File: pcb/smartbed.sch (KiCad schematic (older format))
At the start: 1 part

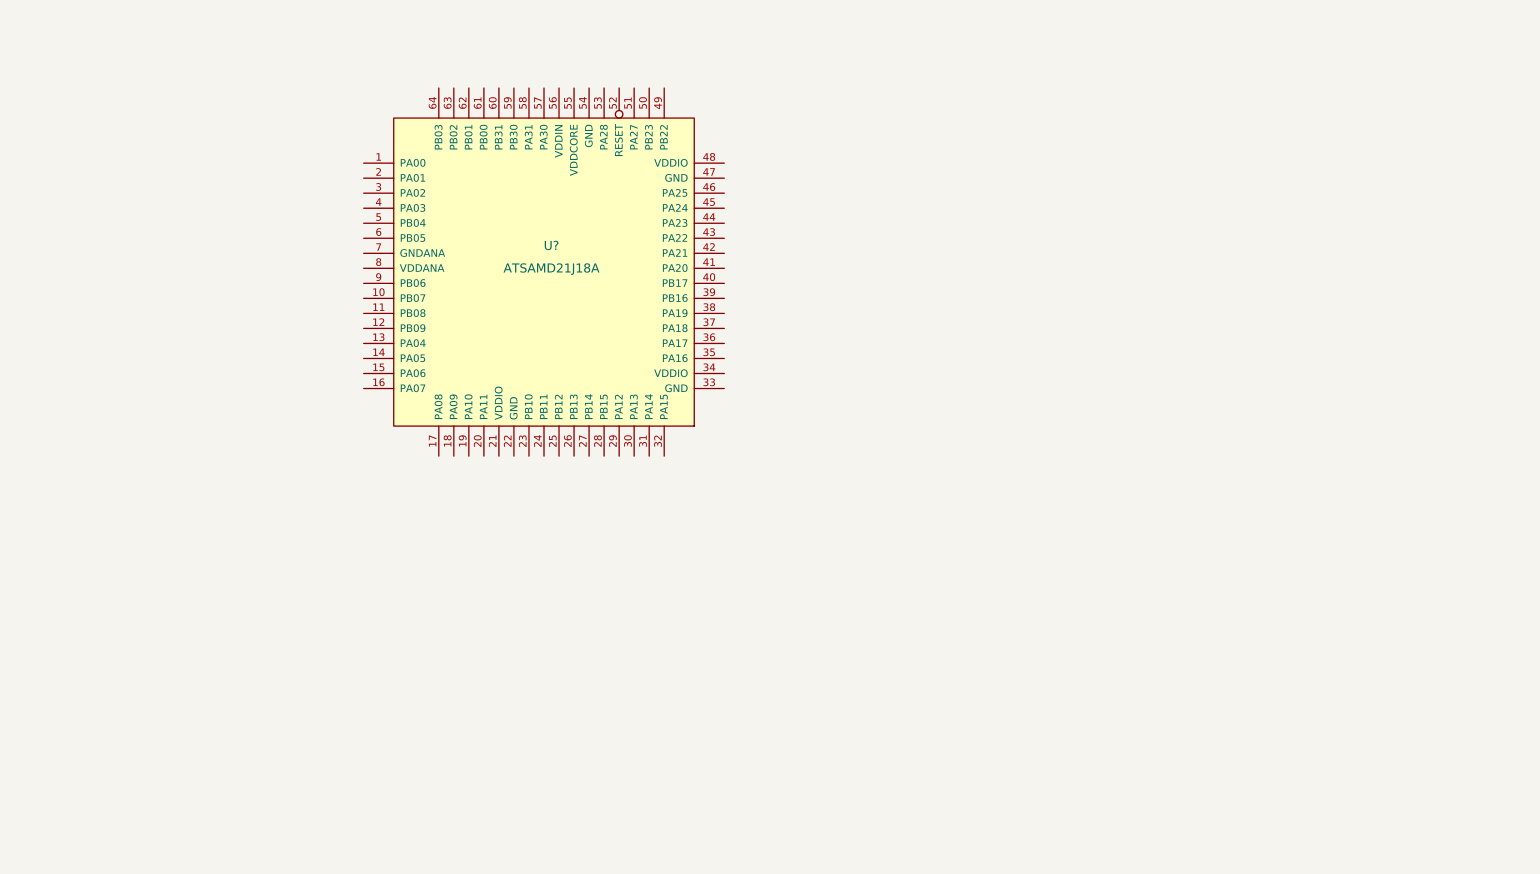
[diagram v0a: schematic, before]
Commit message: Added power supply, USB, internal bus
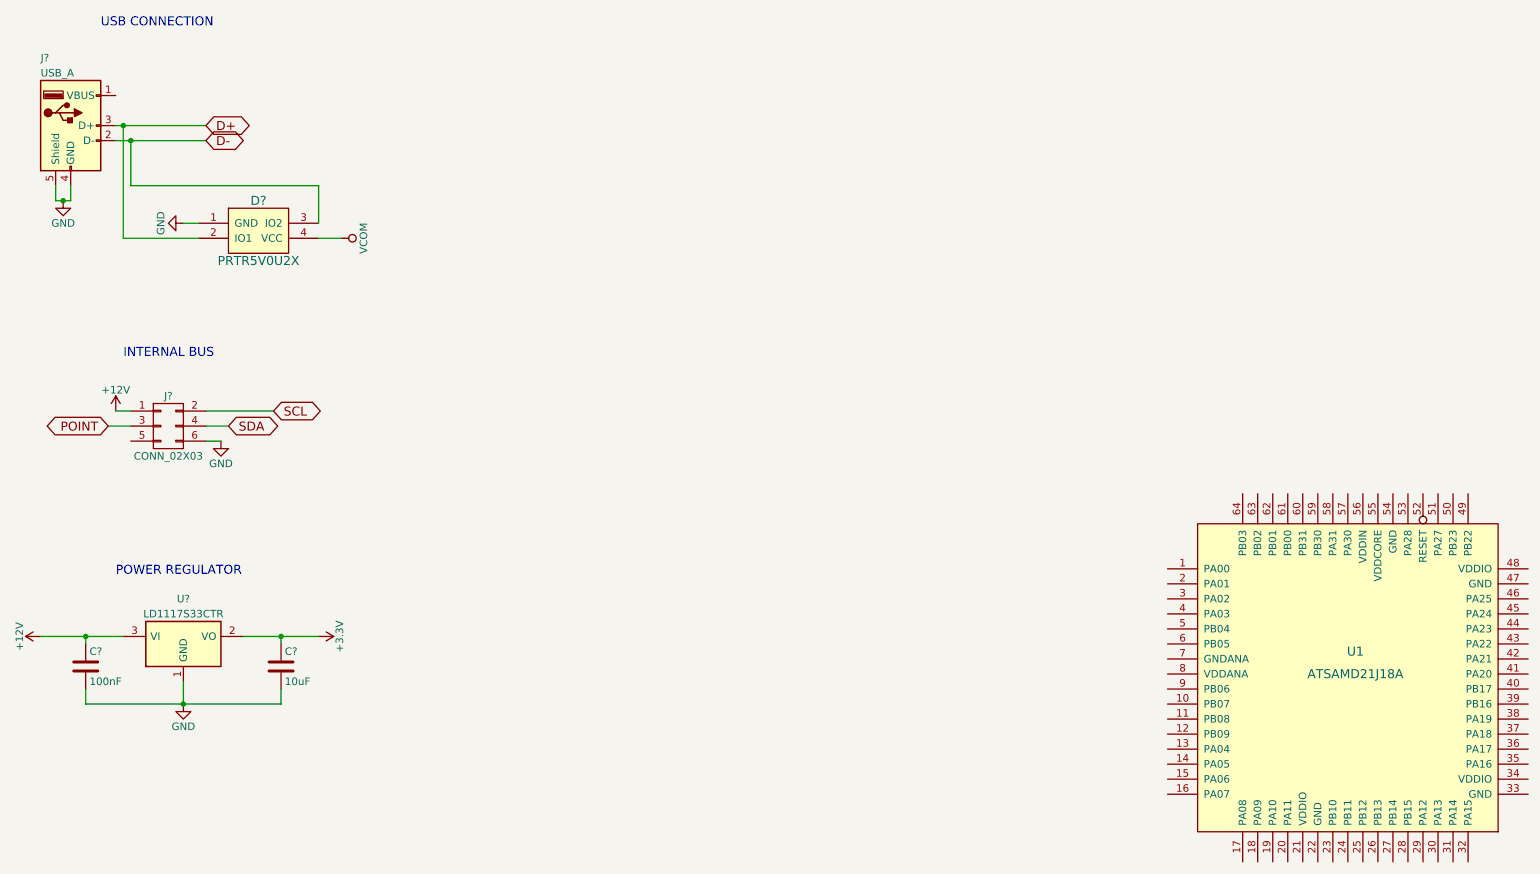
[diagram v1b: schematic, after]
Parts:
- added C?: 10uF, symbol C
- added C?: 100nF, symbol C
- added D?: PRTR5V0U2X, symbol PRTR5V0U2X
- added J?: CONN_02X03, symbol CONN_02X03
- added J?: USB_A, symbol USB_A
- added U?: LD1117S33CTR, TO_SOT_Packages_SMD:SOT-223, symbol LD1117S33CTR
- gave numbers to parts that had none: 1
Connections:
- new net +12V: C?.1, J?.1 (P1), U?.3 (VI)
- new net +3V3: C?.1, U?.2 (VO)
- new net D+: D?.2 (IO1), J?.3 (D+)
- new net D-: D?.3 (IO2), J?.2 (D-)
- new net GND: C?.2, C?.2, D?.1 (GND), J?.4 (GND), J?.5 (Shield), J?.6 (P6), U?.1 (GND)
- new net POINT: J?.3 (P3)
- new net SCL: J?.2 (P2)
- new net SDA: J?.4 (P4)
- new net VCOM: D?.4 (VCC)
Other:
- note added: "INTERNAL BUS"
- note added: "POWER REGULATOR"
- note added: "USB CONNECTION"
- moved on the sheet: U1

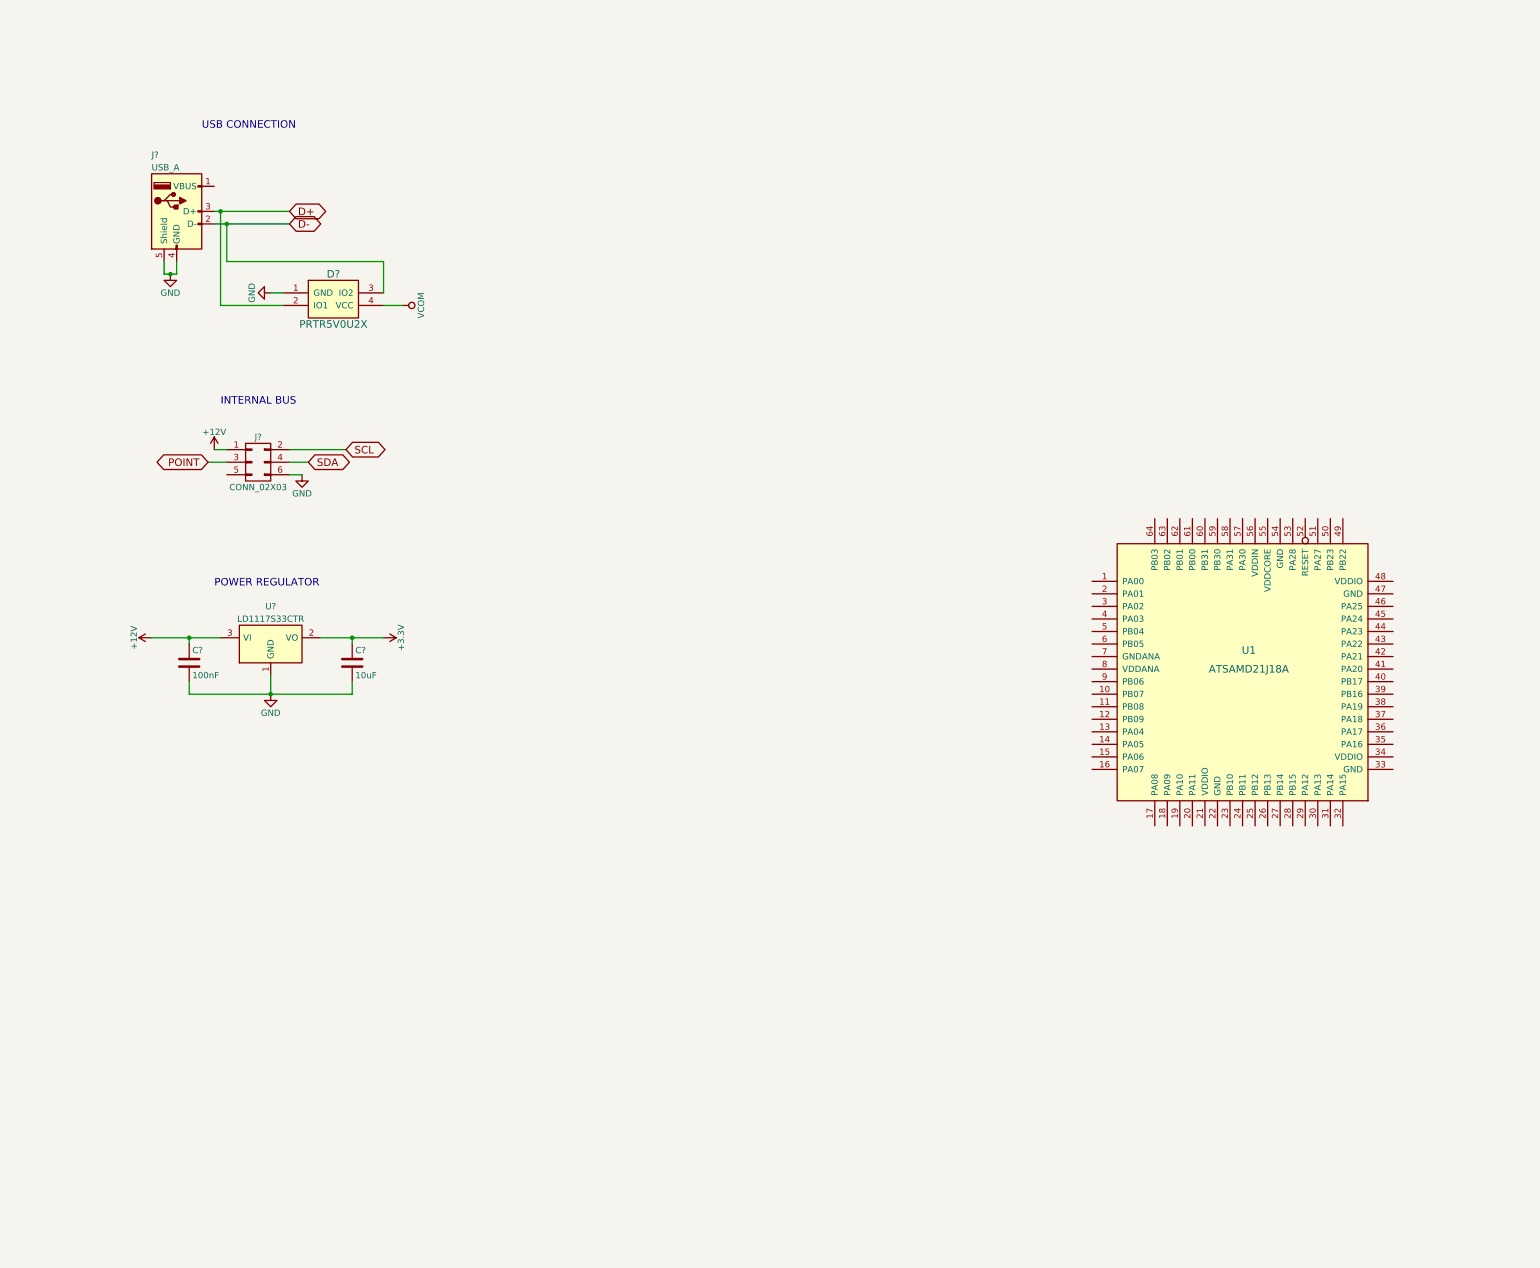
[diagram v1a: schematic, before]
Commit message: Added I2C pull ups, reset button, xtal
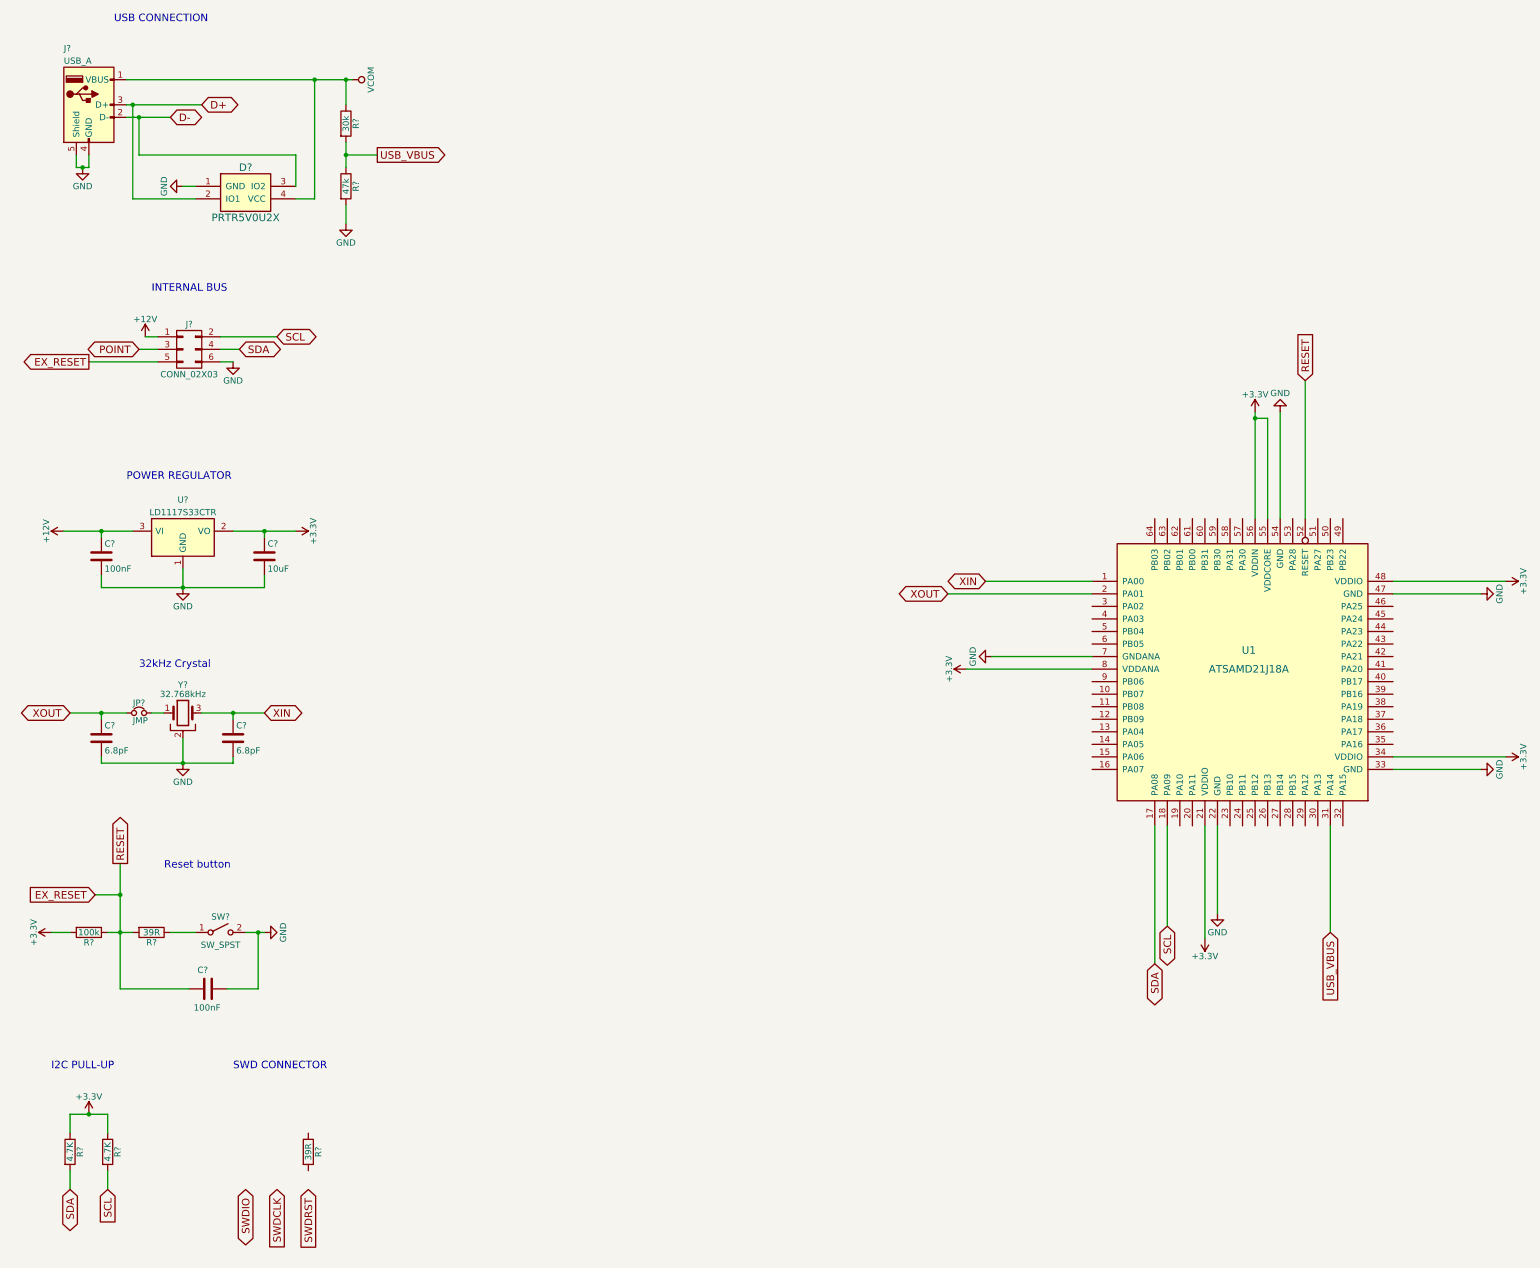
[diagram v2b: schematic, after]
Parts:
- added C? (x2): 6.8pF, symbol C
- added C?: 100nF, symbol C
- added JP?: JMP, symbol Jumper_NC_Small
- added R?: 30k, symbol R
- added R?: 47k, symbol R
- added R?: 100k, symbol R
- added R? (x2): 39R, symbol R
- added R? (x2): 4.7K, symbol R
- added SW?: SW_SPST, symbol SW_SPST
- added Y?: 32.768kHz, symbol Crystal_GND2
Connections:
- net +3V3: now also U1.21 (VDDIO), U1.34 (VDDIO), U1.48 (VDDIO), U1.55 (VDDCORE), U1.56 (VDDIN), U1.8 (VDDANA), R?.1, R?.1, R?.2
- net GND: now also U1.22 (GND), U1.33 (GND), U1.47 (GND), U1.54 (GND), U1.7 (GNDANA), C?.2, C?.2, C?.2, R?.2, SW?.2 (B), Y?.2
- net SCL: now also U1.18 (PA09), R?.2
- net SDA: now also U1.17 (PA08), R?.2
- net VCOM: now also J?.1 (VBUS), R?.1
- net XIN: now reaches U1.1 (PA00)
- net XIN: now also C?.1, Y?.3
- net XOUT: now reaches U1.2 (PA01)
- net XOUT: now also C?.1, JP?.1
- net USB_VBUS: now reaches U1.31 (PA14)
- net USB_VBUS: now also R?.1, R?.2
- net EX_RESET: now reaches U1.52 (RESET)
- net EX_RESET: now also J?.5 (P5), C?.1, R?.1, R?.2
- new net: JP?.2, Y?.1
- new net: R?.1, SW?.1 (A)
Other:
- note added: "32kHz Crystal"
- note added: "I2C PULL-UP"
- note added: "Reset button"
- note added: "SWD CONNECTOR"
- moved on the sheet: C?, D?, J?, U?
